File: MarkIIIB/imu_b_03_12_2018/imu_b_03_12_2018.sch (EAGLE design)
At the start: 12 parts, among them P401 502585-0470, U401 BNO055

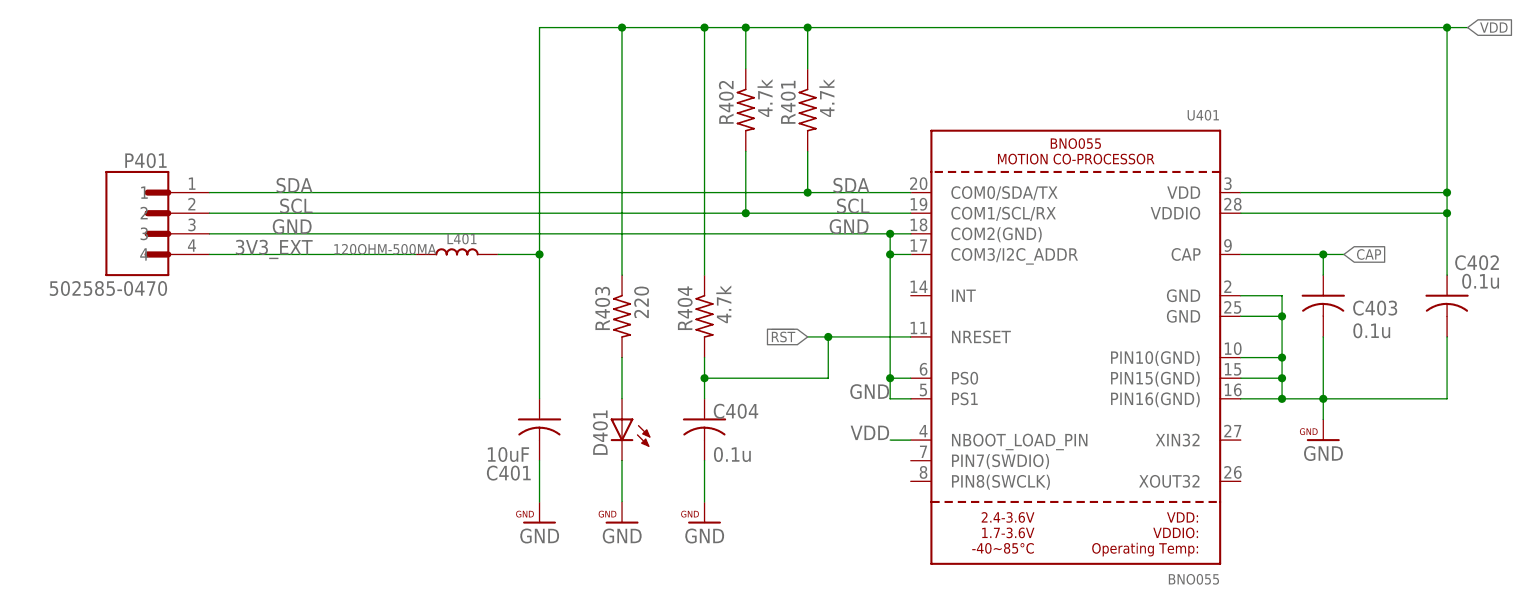
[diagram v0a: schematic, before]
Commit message: Add Part Number ROllup Spreadsheets
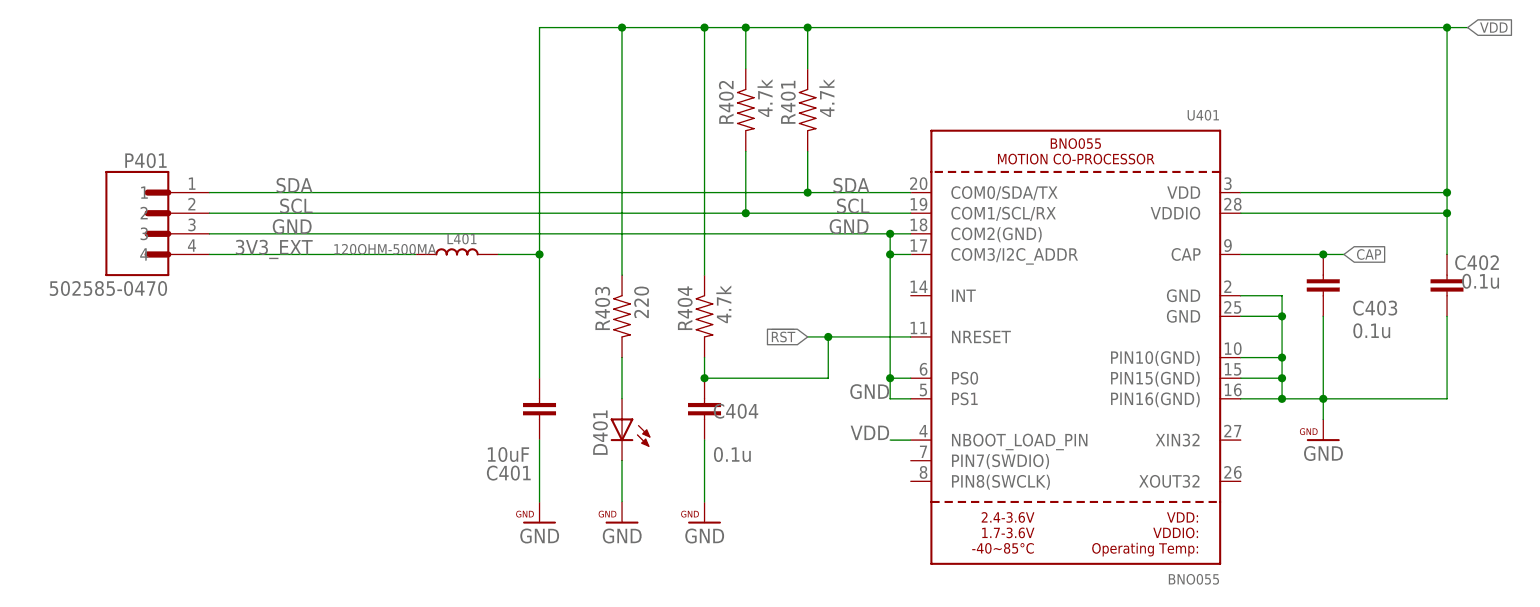
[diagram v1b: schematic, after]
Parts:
- C401, C402, C403, C404: device rcl:C-USC0402 -> PatternAgents-ProtoPads:CAP0402-CAP
- R401, R402, R403, R404: device rcl:R-US_R0402 -> PatternAgents-ProtoPads:RESISTOR0402-TYP
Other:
- moved on the sheet: C401, C402, C403, C404
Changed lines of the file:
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@@
 <part name="U401" library="microbuilder" deviceset="BNO055" device="" value="BNO055"/>
 <part name="P401" library="502585-0470" deviceset="502585-0470" device=""/>
-<part name="C402" library="rcl" deviceset="C-US" device="C0402" value="0.1u"/>
-<part name="C403" library="rcl" deviceset="C-US" device="C0402" value="0.1u"/>
+<part name="C402" library="PatternAgents-ProtoPads" deviceset="CAP" device="0402-CAP" value="0.1u"/>
+<part name="C403" library="PatternAgents-ProtoPads" deviceset="CAP" device="0402-CAP" value="0.1u"/>
 <part name="D401" library="led" deviceset="LED" device="CHIP-LED0603"/>
-<part name="R403" library="rcl" deviceset="R-US_" device="R0402" value="220"/>
+<part name="R403" library="PatternAgents-ProtoPads" deviceset="RESISTOR" device="0402-TYP" value="220"/>
 <part name="FRAME1" library="PatternAgents-Beautify" deviceset="FRAME_ASIZE_LANDSCAPE" device=""/>
-<part name="R402" library="rcl" deviceset="R-US_" device="R0402" value="4.7k"/>
-<part name="R401" library="rcl" deviceset="R-US_" device="R0402" value="4.7k"/>
-<part name="C401" library="rcl" deviceset="C-US" device="C0402" value="10uF"/>
+<part name="R402" library="PatternAgents-ProtoPads" deviceset="RESISTOR" device="0402-TYP" value="4.7k"/>
+<part name="R401" library="PatternAgents-ProtoPads" deviceset="RESISTOR" device="0402-TYP" value="4.7k"/>
+<part name="C401" library="PatternAgents-ProtoPads" deviceset="CAP" device="0402-CAP" value="10uF"/>
 <part name="L401" library="halcyonmod_Passives" deviceset="SMD-FERRITE-CHIP-120-OHM-500MA(0603)" device="" value="120OHM-500MA"/>
 <part name="U$2" library="PatternAgents-Beautify" deviceset="GND" device=""/>
 <part name="U$5" library="PatternAgents-Beautify" deviceset="GND" device=""/>
 <part name="U$6" library="PatternAgents-Beautify" deviceset="GND" device=""/>
-<part name="C404" library="rcl" deviceset="C-US" device="C0402" value="0.1u"/>
-<part name="R404" library="rcl" deviceset="R-US_" device="R0402" value="4.7k"/>
+<part name="C404" library="PatternAgents-ProtoPads" deviceset="CAP" device="0402-CAP" value="0.1u"/>
+<part name="R404" library="PatternAgents-ProtoPads" deviceset="RESISTOR" device="0402-TYP" value="4.7k"/>
 <part name="U$8" library="PatternAgents-Beautify" deviceset="GND" device=""/>
 </parts>
@@
 </instance>
 <instance part="D401" gate="G$1" x="106.68" y="101.6" rot="MR0"/>
-<instance part="R403" gate="G$1" x="106.68" y="114.3" rot="MR270"/>
+<instance part="R403" gate="R" x="106.68" y="114.3" rot="MR270"/>
 <instance part="FRAME1" gate="G$2" x="172.72" y="0"/>
 <instance part="FRAME1" gate="G$1" x="0" y="0"/>
-<instance part="R402" gate="G$1" x="121.92" y="139.7" rot="MR270"/>
-<instance part="R401" gate="G$1" x="129.54" y="139.7" rot="MR270"/>
+<instance part="R402" gate="R" x="121.92" y="139.7" rot="MR270"/>
+<instance part="R401" gate="R" x="129.54" y="139.7" rot="MR270"/>
 <instance part="C401" gate="G$1" x="96.52" y="101.6" smashed="yes" rot="MR0">
 <attribute name="NAME" x="89.916" y="95.885" size="1.778" layer="95" rot="MR180"/>
@@
 <attribute name="VALUE" x="117.856" y="98.171" size="1.778" layer="96" rot="MR180"/>
 </instance>
-<instance part="R404" gate="G$1" x="116.84" y="114.3" rot="MR270"/>
+<instance part="R404" gate="R" x="116.84" y="114.3" rot="MR270"/>
 <instance part="U$8" gate="G$1" x="116.84" y="91.44" rot="MR0"/>
 </instances>
@@
 <wire x1="187.96" y1="104.14" x2="182.88" y2="104.14" width="0.1524" layer="91"/>
 <pinref part="C403" gate="G$1" pin="2"/>
-<wire x1="193.04" y1="111.76" x2="193.04" y2="104.14" width="0.1524" layer="91"/>
+<wire x1="193.04" y1="114.3" x2="193.04" y2="104.14" width="0.1524" layer="91"/>
 <wire x1="193.04" y1="104.14" x2="187.96" y2="104.14" width="0.1524" layer="91"/>
 <junction x="187.96" y="104.14"/>
@@
 <pinref part="C402" gate="G$1" pin="2"/>
 <wire x1="193.04" y1="104.14" x2="208.28" y2="104.14" width="0.1524" layer="91"/>
-<wire x1="208.28" y1="104.14" x2="208.28" y2="111.76" width="0.1524" layer="91"/>
+<wire x1="208.28" y1="104.14" x2="208.28" y2="114.3" width="0.1524" layer="91"/>
 <pinref part="U401" gate="G$1" pin="GND@1"/>
 <wire x1="182.88" y1="116.84" x2="187.96" y2="116.84" width="0.1524" layer="91"/>
@@
 <segment>
 <pinref part="C401" gate="G$1" pin="2"/>
-<wire x1="96.52" y1="91.44" x2="96.52" y2="96.52" width="0.1524" layer="91"/>
+<wire x1="96.52" y1="91.44" x2="96.52" y2="99.06" width="0.1524" layer="91"/>
 <pinref part="U$6" gate="G$1" pin="GND"/>
 </segment>
@@
 <pinref part="U$8" gate="G$1" pin="GND"/>
 <pinref part="C404" gate="G$1" pin="2"/>
-<wire x1="116.84" y1="96.52" x2="116.84" y2="91.44" width="0.1524" layer="91"/>
+<wire x1="116.84" y1="99.06" x2="116.84" y2="91.44" width="0.1524" layer="91"/>
 </segment>
 </net>
@@
 <wire x1="195.58" y1="121.92" x2="193.04" y2="121.92" width="0.1524" layer="91"/>
 <wire x1="193.04" y1="121.92" x2="182.88" y2="121.92" width="0.1524" layer="91"/>
-<wire x1="193.04" y1="119.38" x2="193.04" y2="121.92" width="0.1524" layer="91"/>
 <junction x="193.04" y="121.92"/>
 </segment>
@@
 <pinref part="U401" gate="G$1" pin="COM0/SDA/TX"/>
 <label x="137.16" y="129.54" size="1.778" layer="95" rot="MR0"/>
-<pinref part="R401" gate="G$1" pin="2"/>
+<pinref part="R401" gate="R" pin="2"/>
 <wire x1="142.24" y1="129.54" x2="129.54" y2="129.54" width="0.1524" layer="91"/>
 <wire x1="129.54" y1="129.54" x2="129.54" y2="134.62" width="0.1524" layer="91"/>
@@
 <pinref part="U401" gate="G$1" pin="COM1/SCL/RX"/>
 <label x="137.16" y="127" size="1.778" layer="95" rot="MR0"/>
-<pinref part="R402" gate="G$1" pin="2"/>
+<pinref part="R402" gate="R" pin="2"/>
 <wire x1="142.24" y1="127" x2="121.92" y2="127" width="0.1524" layer="91"/>
 <wire x1="121.92" y1="127" x2="121.92" y2="134.62" width="0.1524" layer="91"/>
@@
 <net name="N$2" class="0">
 <segment>
-<pinref part="R403" gate="G$1" pin="2"/>
+<pinref part="R403" gate="R" pin="2"/>
 <pinref part="D401" gate="G$1" pin="A"/>
 <wire x1="106.68" y1="109.22" x2="106.68" y2="104.14" width="0.1524" layer="91"/>
@@
 <pinref part="C402" gate="G$1" pin="1"/>
 <wire x1="182.88" y1="127" x2="208.28" y2="127" width="0.1524" layer="91"/>
-<wire x1="208.28" y1="127" x2="208.28" y2="119.38" width="0.1524" layer="91"/>
+<wire x1="208.28" y1="127" x2="208.28" y2="121.92" width="0.1524" layer="91"/>
 <pinref part="U401" gate="G$1" pin="VDD"/>
 <wire x1="182.88" y1="129.54" x2="208.28" y2="129.54" width="0.1524" layer="91"/>
@@
 <wire x1="106.68" y1="149.86" x2="106.68" y2="119.38" width="0.1524" layer="91"/>
 <pinref part="L401" gate="L" pin="1"/>
-<pinref part="R402" gate="G$1" pin="1"/>
+<pinref part="R402" gate="R" pin="1"/>
 <wire x1="96.52" y1="121.92" x2="91.44" y2="121.92" width="0.1524" layer="91"/>
 <wire x1="121.92" y1="144.78" x2="121.92" y2="149.86" width="0.1524" layer="91"/>
 <junction x="121.92" y="149.86"/>
-<pinref part="R401" gate="G$1" pin="1"/>
+<pinref part="R401" gate="R" pin="1"/>
 <wire x1="129.54" y1="144.78" x2="129.54" y2="149.86" width="0.1524" layer="91"/>
 <junction x="129.54" y="149.86"/>
-<pinref part="R403" gate="G$1" pin="1"/>
+<pinref part="R403" gate="R" pin="1"/>
 <label x="210.82" y="149.86" size="1.27" layer="95" font="vector" ratio="10" rot="MR180" xref="yes"/>
 <wire x1="106.68" y1="149.86" x2="96.52" y2="149.86" width="0.1524" layer="91"/>
 <junction x="106.68" y="149.86"/>
-<pinref part="R404" gate="G$1" pin="1"/>
+<pinref part="R404" gate="R" pin="1"/>
 <wire x1="116.84" y1="119.38" x2="116.84" y2="149.86" width="0.1524" layer="91"/>
 <junction x="116.84" y="149.86"/>
 <pinref part="C401" gate="G$1" pin="1"/>
-<wire x1="96.52" y1="104.14" x2="96.52" y2="121.92" width="0.1524" layer="91"/>
+<wire x1="96.52" y1="106.68" x2="96.52" y2="121.92" width="0.1524" layer="91"/>
 <junction x="96.52" y="121.92"/>
 <wire x1="96.52" y1="121.92" x2="96.52" y2="149.86" width="0.1524" layer="91"/>
@@
 <net name="!RST" class="0">
 <segment>
-<pinref part="R404" gate="G$1" pin="2"/>
+<pinref part="R404" gate="R" pin="2"/>
 <pinref part="C404" gate="G$1" pin="1"/>
 <wire x1="116.84" y1="109.22" x2="116.84" y2="106.68" width="0.1524" layer="91"/>
 <pinref part="U401" gate="G$1" pin="NRESET"/>
-<wire x1="116.84" y1="106.68" x2="116.84" y2="104.14" width="0.1524" layer="91"/>
 <wire x1="142.24" y1="111.76" x2="132.08" y2="111.76" width="0.1524" layer="91"/>
 <wire x1="132.08" y1="111.76" x2="132.08" y2="106.68" width="0.1524" layer="91"/>
